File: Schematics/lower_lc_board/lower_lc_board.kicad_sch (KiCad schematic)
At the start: 0 parts

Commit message: more organizational work, add shared footprint, model, symbol dirs and clean up individuals
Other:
- title: Lower Control Board -> HYDRA | Lower Control Board
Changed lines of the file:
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@@
 	(paper "A4")
 	(title_block
-		(title "Lower Control Board")
+		(title "HYDRA | Lower Control Board")
 		(rev "A")
 		(company "Queen's Rocket Engineering Team")

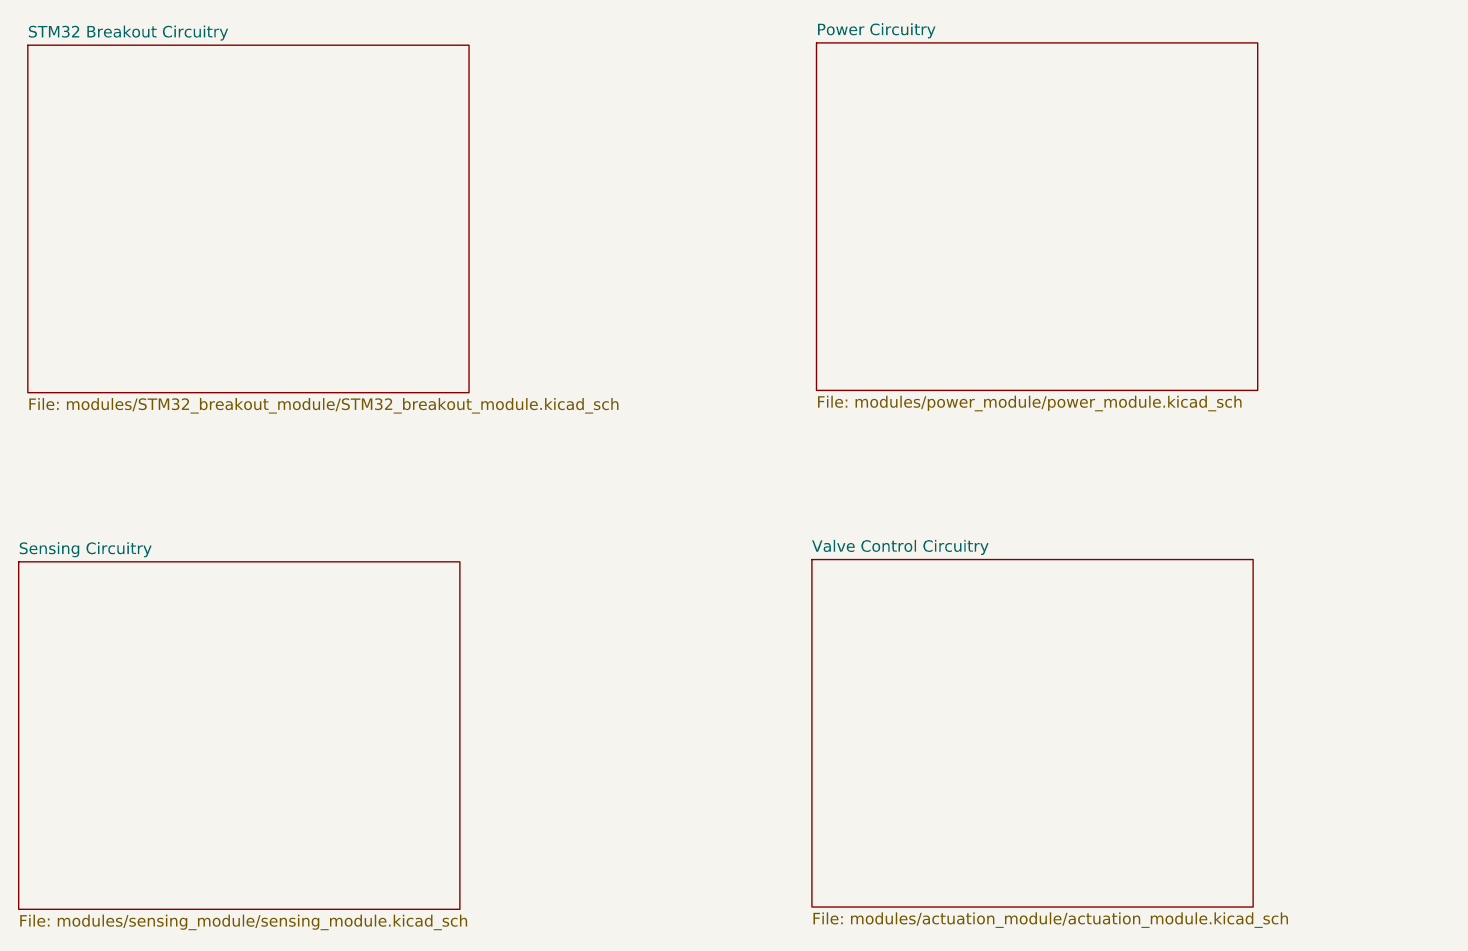
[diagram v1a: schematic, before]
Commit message: organize working copy of lower valve board for merge to main
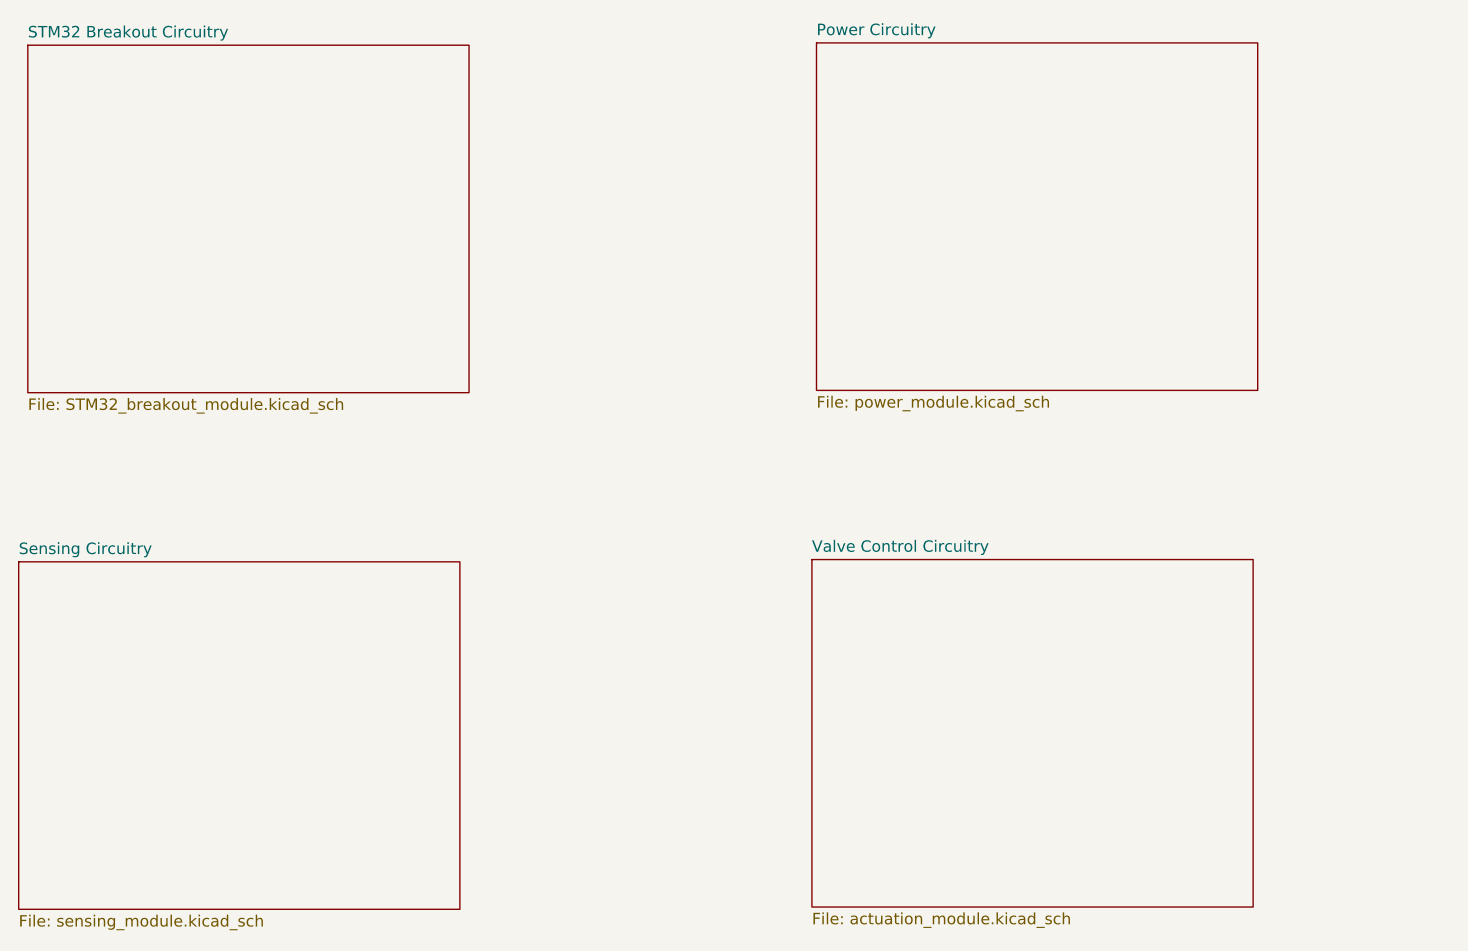
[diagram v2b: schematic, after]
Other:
- sheet Power Circuitry: file modules/power_module/power_module.kicad_sch -> power_module.kicad_sch
- sheet STM32 Breakout Circuitry: file modules/STM32_breakout_module/STM32_breakout_module.kicad_sch -> STM32_breakout_module.kicad_sch
- sheet Sensing Circuitry: file modules/sensing_module/sensing_module.kicad_sch -> sensing_module.kicad_sch
- sheet Valve Control Circuitry: file modules/actuation_module/actuation_module.kicad_sch -> actuation_module.kicad_sch
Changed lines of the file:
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@@
 			)
 		)
-		(property "Sheetfile" "modules/actuation_module/actuation_module.kicad_sch"
+		(property "Sheetfile" "actuation_module.kicad_sch"
 			(at 159.258 139.0146 0)
 			(effects
@@
 			)
 		)
-		(property "Sheetfile" "modules/STM32_breakout_module/STM32_breakout_module.kicad_sch"
+		(property "Sheetfile" "STM32_breakout_module.kicad_sch"
 			(at 72.136 81.8646 0)
 			(effects
@@
 			)
 		)
-		(property "Sheetfile" "modules/sensing_module/sensing_module.kicad_sch"
+		(property "Sheetfile" "sensing_module.kicad_sch"
 			(at 71.12 139.2686 0)
 			(effects
@@
 			)
 		)
-		(property "Sheetfile" "modules/power_module/power_module.kicad_sch"
+		(property "Sheetfile" "power_module.kicad_sch"
 			(at 159.766 81.6106 0)
 			(effects

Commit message: updates and added to cart
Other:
- title: HYDRA | Lower Control Board -> QRET 25-26 SRAD Hyrbid Lower Control Module
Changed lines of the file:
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@@
 	(paper "A4")
 	(title_block
-		(title "HYDRA | Lower Control Board")
-		(rev "A")
+		(title "QRET 25-26 SRAD Hyrbid Lower Control Module")
+		(rev "V1.0")
 		(company "Queen's Rocket Engineering Team")
 		(comment 1 "Jeevan Sanchez")

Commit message: add board-specifc READMEs (TODO), cleanup schematic titles
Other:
- title: QRET 25-26 SRAD Hyrbid Lower Control Module -> QRET 25-26 SRAD Hybrid Lower Control Module
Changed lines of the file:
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@@
 	(paper "A4")
 	(title_block
-		(title "QRET 25-26 SRAD Hyrbid Lower Control Module")
+		(title "QRET 25-26 SRAD Hybrid Lower Control Module")
 		(rev "V1.0")
 		(company "Queen's Rocket Engineering Team")
-		(comment 1 "Jeevan Sanchez")
+		(comment 1 "Contributors: Jeevan Sanchez, Tristan Alderson")
 	)
 	(sheet
